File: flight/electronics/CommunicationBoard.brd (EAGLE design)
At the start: 90 x 90 mm, 11 parts, among them J1 CONUFL001-SMD-T, X1 JST-XH-02-PIN

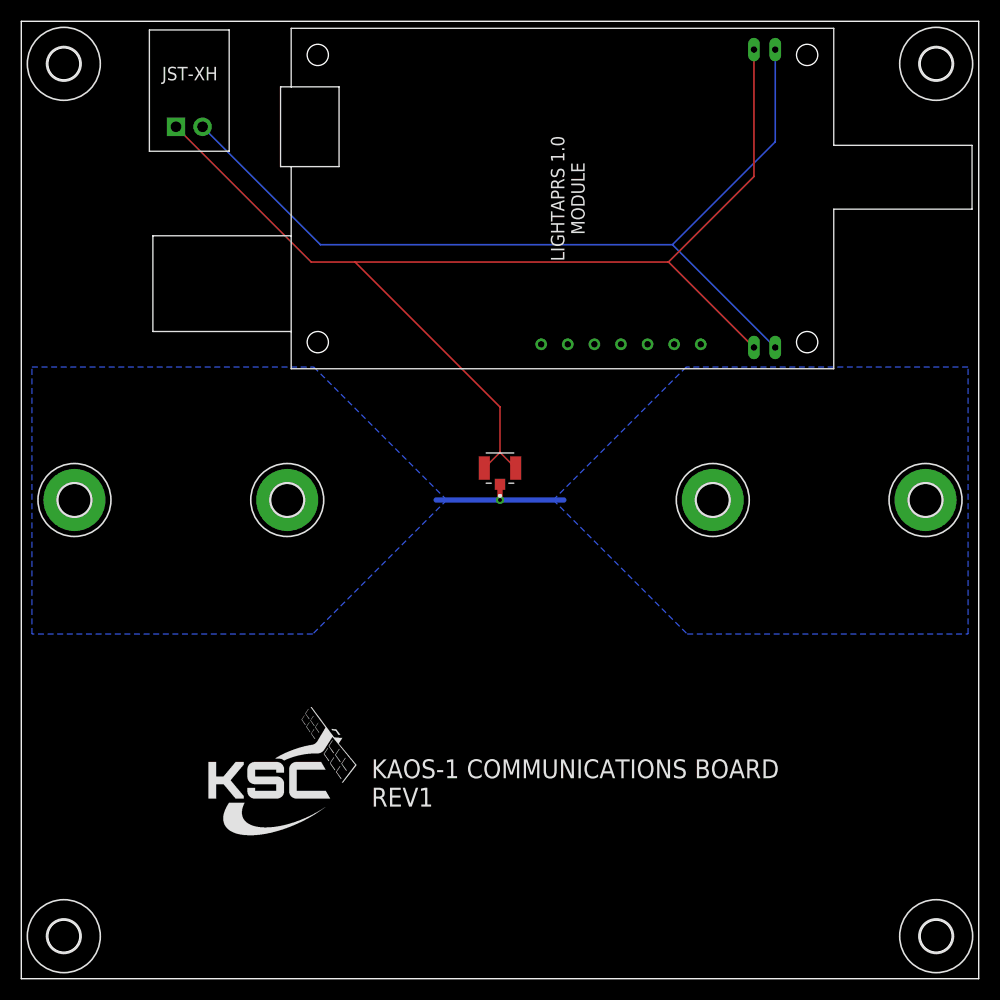
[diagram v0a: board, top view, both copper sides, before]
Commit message: move antenna mounting holes
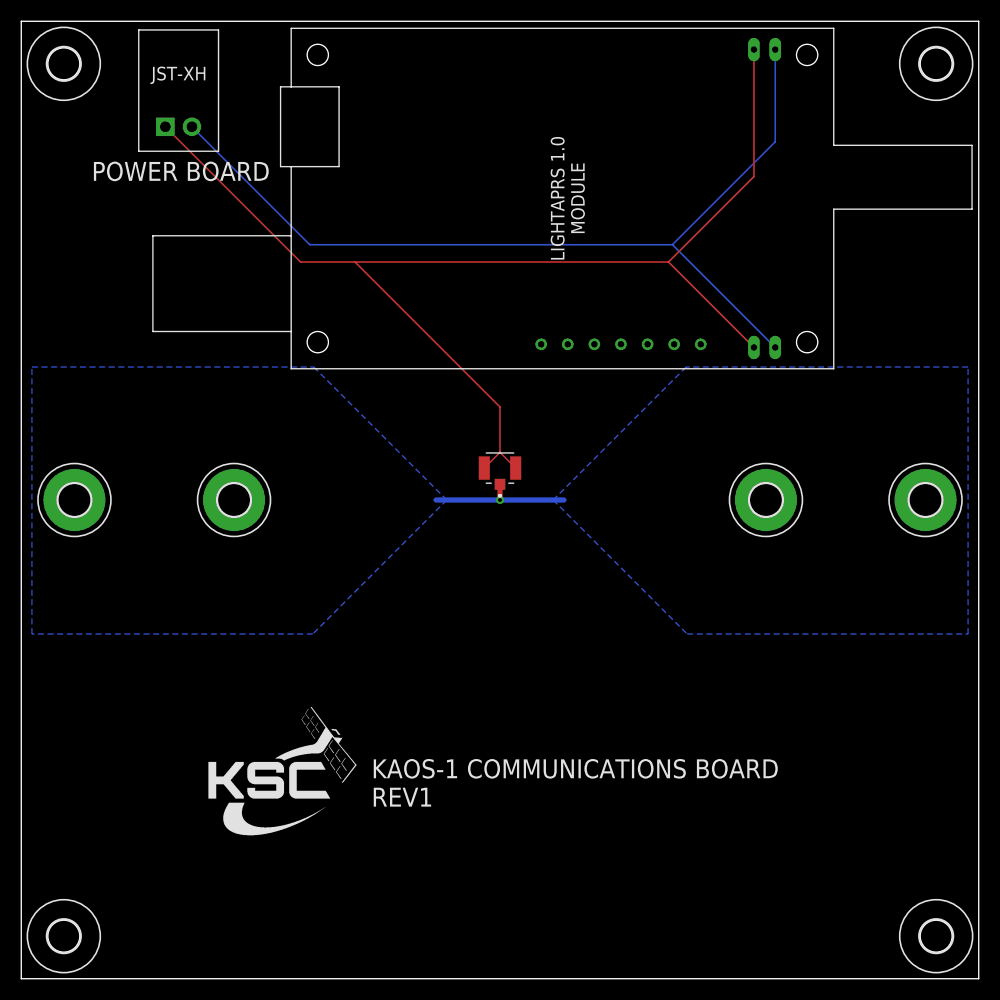
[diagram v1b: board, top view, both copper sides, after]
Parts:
- moved H2 5.00 mm to (70.0, 45.0)
- moved H3 5.00 mm to (20.0, 45.0)
- moved X1 1.00 mm to (13.5, 80.1)
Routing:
- net VBAT: track 84.8 -> 85.8 mm
- net GND: track 113.9 -> 114.9 mm
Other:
- board text added: "POWER BOARD"
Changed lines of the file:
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@@
 <rectangle x1="27.2161" y1="25.4889" x2="27.3177" y2="25.5143" layer="21"/>
 <rectangle x1="27.1907" y1="25.5143" x2="27.3177" y2="25.5397" layer="21"/>
+<text x="15" y="75" size="1.778" layer="21" font="vector" align="bottom-center">POWER BOARD</text>
 </plain>
 <attributes>
@@
 <elements>
 <element name="U$1" library="Breakouts" package="LIGHTAPRS" value="LIGHTAPRS" x="51.372" y="73.3382" smashed="yes" rot="R270"/>
-<element name="X1" library="Rembrandt Electronics - JST XH Connectors v1-0" package="JST-XH_S2B" value="JST-XH-02-PIN" x="14.5424" y="80.0828" smashed="yes"/>
+<element name="X1" library="Rembrandt Electronics - JST XH Connectors v1-0" package="JST-XH_S2B" value="JST-XH-02-PIN" x="13.5424" y="80.0828" smashed="yes"/>
 <element name="J1" library="CONUFL001-SMD-T" package="LINX_CONUFL001-SMD-T" value="CONUFL001-SMD-T" x="45" y="48" smashed="yes">
 <attribute name="AVAILABILITY" value="In Stock" x="45" y="48" size="1.778" layer="27" display="off"/>
@@
 <attribute name="POPULARITY" value="17" x="85" y="45" size="0.0508" layer="27" font="vector" display="off"/>
 </element>
-<element name="H2" library="holes" library_urn="urn:adsk.eagle:library:237" package="3,0-PAD" package3d_urn="urn:adsk.eagle:package:14280/1" value="MOUNT-PAD-ROUND3.0" x="65" y="45" smashed="yes">
-<attribute name="POPULARITY" value="17" x="65" y="45" size="0.0508" layer="27" font="vector" display="off"/>
-</element>
-<element name="H3" library="holes" library_urn="urn:adsk.eagle:library:237" package="3,0-PAD" package3d_urn="urn:adsk.eagle:package:14280/1" value="MOUNT-PAD-ROUND3.0" x="25" y="45" smashed="yes">
-<attribute name="POPULARITY" value="17" x="25" y="45" size="0.0508" layer="27" font="vector" display="off"/>
+<element name="H2" library="holes" library_urn="urn:adsk.eagle:library:237" package="3,0-PAD" package3d_urn="urn:adsk.eagle:package:14280/1" value="MOUNT-PAD-ROUND3.0" x="70" y="45" smashed="yes">
+<attribute name="POPULARITY" value="17" x="70" y="45" size="0.0508" layer="27" font="vector" display="off"/>
+</element>
+<element name="H3" library="holes" library_urn="urn:adsk.eagle:library:237" package="3,0-PAD" package3d_urn="urn:adsk.eagle:package:14280/1" value="MOUNT-PAD-ROUND3.0" x="20" y="45" smashed="yes">
+<attribute name="POPULARITY" value="17" x="20" y="45" size="0.0508" layer="27" font="vector" display="off"/>
 </element>
 <element name="H4" library="holes" library_urn="urn:adsk.eagle:library:237" package="3,0-PAD" package3d_urn="urn:adsk.eagle:package:14280/1" value="MOUNT-PAD-ROUND3.0" x="5" y="45" smashed="yes">
@@
 <contactref element="U$1" pad="GND2"/>
 <contactref element="X1" pad="PIN1"/>
-<wire x1="14.5424" y1="80.0828" x2="27.2552" y2="67.37" width="0.1524" layer="1"/>
+<wire x1="13.5424" y1="80.0828" x2="26.2552" y2="67.37" width="0.1524" layer="1"/>
 <wire x1="31.37" y1="67.37" x2="45" y2="53.74" width="0.1524" layer="1"/>
 <contactref element="J1" pad="3"/>
@@
 <wire x1="46.475" y1="48" x2="45" y2="49.475" width="0.1524" layer="1"/>
 <wire x1="45" y1="49.475" x2="45" y2="53.74" width="0.1524" layer="1"/>
-<wire x1="31.37" y1="67.37" x2="27.2552" y2="67.37" width="0.1524" layer="1"/>
+<wire x1="31.37" y1="67.37" x2="26.2552" y2="67.37" width="0.1524" layer="1"/>
 <wire x1="68.872" y1="59.3382" x2="60.8402" y2="67.37" width="0.1524" layer="1"/>
 <wire x1="60.8402" y1="67.37" x2="31.37" y2="67.37" width="0.1524" layer="1"/>
@@
 <contactref element="U$1" pad="VBAT1"/>
 <contactref element="U$1" pad="VBAT2"/>
-<wire x1="28.1252" y1="69" x2="17.0424" y2="80.0828" width="0.1524" layer="16"/>
-<wire x1="61.2102" y1="69" x2="28.1252" y2="69" width="0.1524" layer="16"/>
+<wire x1="27.1252" y1="69" x2="16.0424" y2="80.0828" width="0.1524" layer="16"/>
+<wire x1="61.2102" y1="69" x2="27.1252" y2="69" width="0.1524" layer="16"/>
 <wire x1="70.872" y1="59.3382" x2="61.2102" y2="69" width="0.1524" layer="16"/>
 <wire x1="70.872" y1="78.6618" x2="61.2102" y2="69" width="0.1524" layer="16"/>

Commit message: round board corners
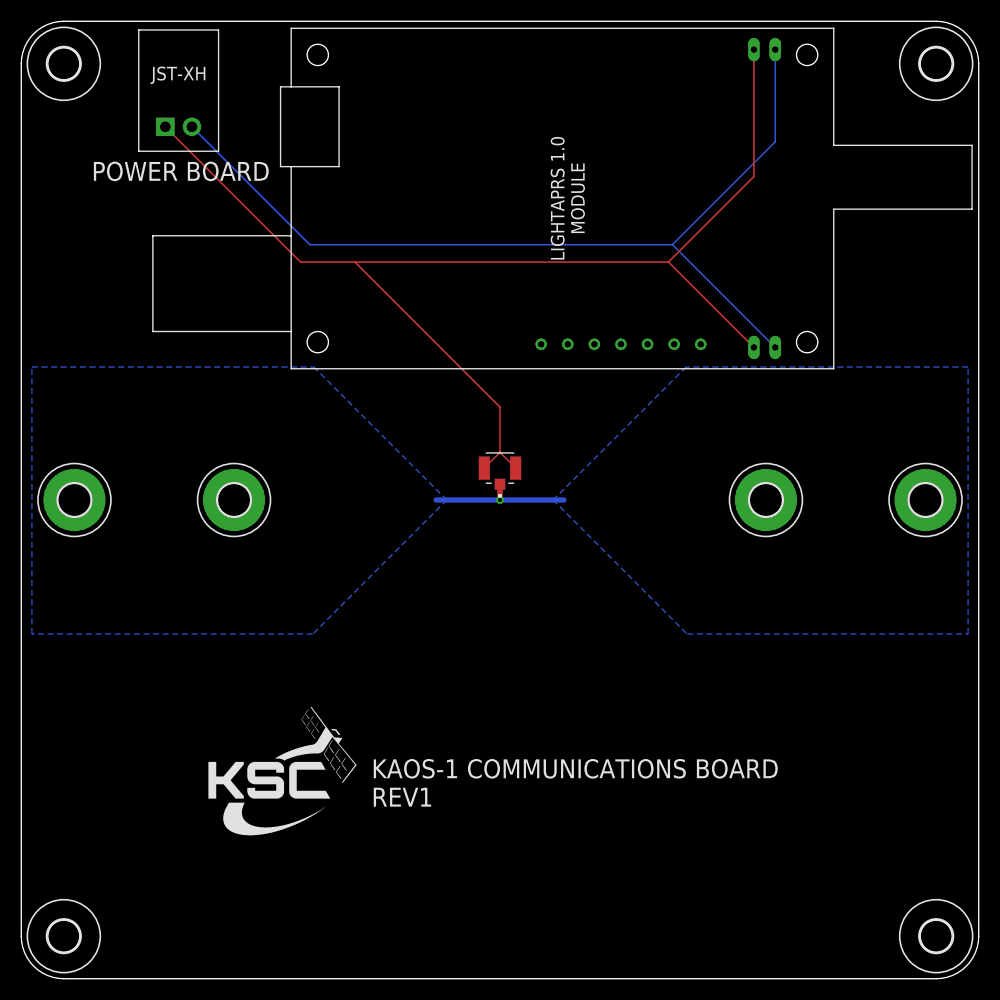
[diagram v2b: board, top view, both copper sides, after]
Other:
- outline, holes or cut-outs redrawn
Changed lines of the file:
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@@
 <board>
 <plain>
-<wire x1="0" y1="0" x2="90" y2="0" width="0" layer="20"/>
-<wire x1="90" y1="0" x2="90" y2="90" width="0" layer="20"/>
-<wire x1="90" y1="90" x2="0" y2="90" width="0" layer="20"/>
-<wire x1="0" y1="90" x2="0" y2="0" width="0" layer="20"/>
+<wire x1="4" y1="0" x2="86" y2="0" width="0" layer="20"/>
+<wire x1="90" y1="4" x2="90" y2="86" width="0" layer="20"/>
+<wire x1="86" y1="90" x2="4" y2="90" width="0" layer="20"/>
 <polygon width="0.2" layer="30">
 <vertex x="1" y="32.4"/>
@@
 <rectangle x1="27.1907" y1="25.5143" x2="27.3177" y2="25.5397" layer="21"/>
 <text x="15" y="75" size="1.778" layer="21" font="vector" align="bottom-center">POWER BOARD</text>
+<wire x1="0" y1="86" x2="0" y2="4" width="0" layer="20"/>
+<wire x1="4" y1="0" x2="0" y2="4" width="0" layer="20" curve="-90"/>
+<wire x1="90" y1="4" x2="86" y2="0" width="0" layer="20" curve="-90"/>
+<wire x1="86" y1="90" x2="90" y2="86" width="0" layer="20" curve="-90"/>
+<wire x1="0" y1="86" x2="4" y2="90" width="0" layer="20" curve="-90"/>
 </plain>
 <attributes>

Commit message: remove thermal isolation
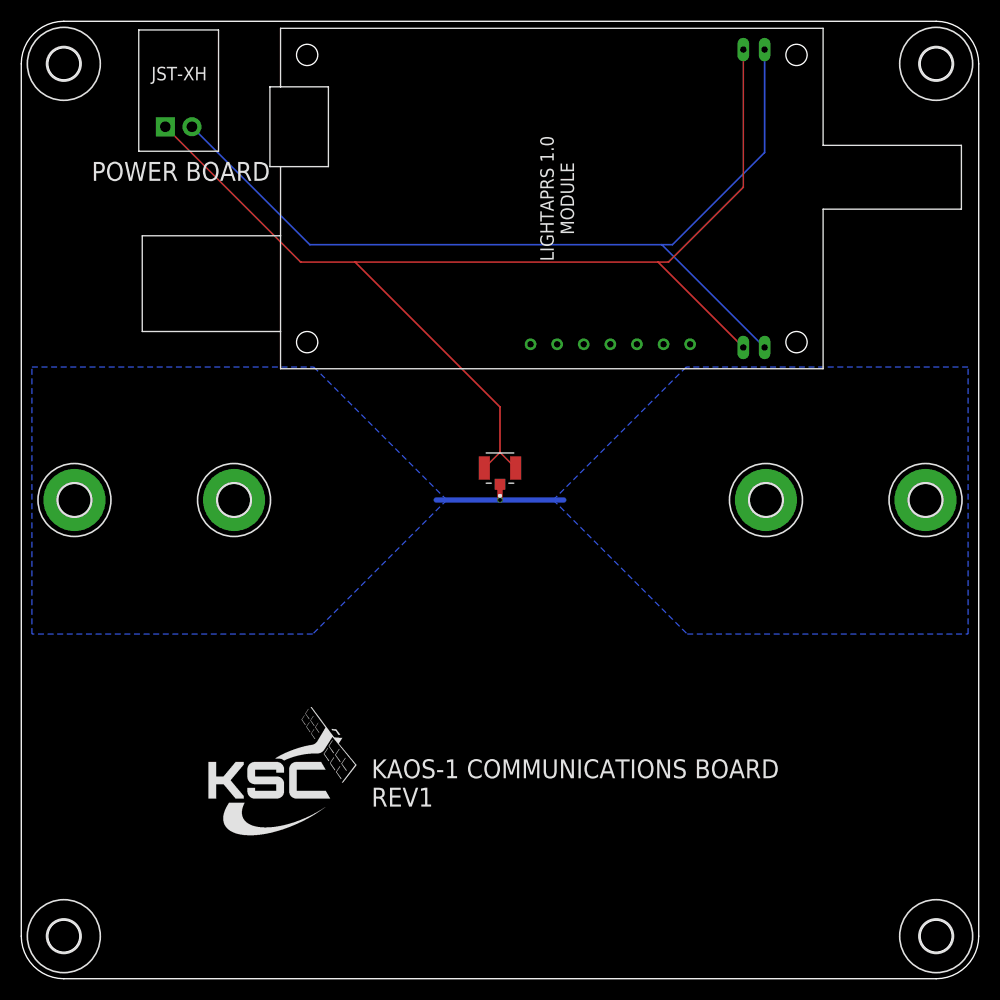
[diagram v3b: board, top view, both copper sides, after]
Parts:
- moved U$1 1.00 mm to (50.4, 73.3)
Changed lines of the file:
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@@
 </class>
 </classes>
-<designrules name="default">
-<description language="de">&lt;b&gt;EAGLE Design Rules&lt;/b&gt;
-&lt;p&gt;
-Die Standard-Design-Rules sind so gewählt, dass sie für
-die meisten Anwendungen passen. Sollte ihre Platine
-besondere Anforderungen haben, treffen Sie die erforderlichen
-Einstellungen hier und speichern die Design Rules unter
-einem neuen Namen ab.</description>
-<description language="en">&lt;b&gt;EAGLE Design Rules&lt;/b&gt;
-&lt;p&gt;
-The default Design Rules have been set to cover
-a wide range of applications. Your particular design
-may have different requirements, so please make the
-necessary adjustments and save your customized
-design rules under a new name.</description>
+<designrules name="jlcpcb-2layers">
+<description language="en">&lt;b&gt;JLCPCB design rules (2 layers)&lt;/b&gt;
+&lt;ul&gt;
+&lt;li&gt;Board thickness: 1.6mm&lt;/li&gt;
+&lt;li&gt;Copper weight: 1oz (35um)&lt;/li&gt;
+&lt;li&gt;Note: annular ring aren't minimal&lt;/li&gt;
+&lt;/ul&gt;</description>
 <param name="layerSetup" value="(1*16)"/>
 <param name="mtCopper" value="0.035mm 0.035mm 0.035mm 0.035mm 0.035mm 0.035mm 0.035mm 0.035mm 0.035mm 0.035mm 0.035mm 0.035mm 0.035mm 0.035mm 0.035mm 0.035mm"/>
-<param name="mtIsolate" value="1.5mm 0.15mm 0.2mm 0.15mm 0.2mm 0.15mm 0.2mm 0.15mm 0.2mm 0.15mm 0.2mm 0.15mm 0.2mm 0.15mm 0.2mm"/>
-<param name="mdWireWire" value="6mil"/>
-<param name="mdWirePad" value="6mil"/>
-<param name="mdWireVia" value="6mil"/>
-<param name="mdPadPad" value="6mil"/>
-<param name="mdPadVia" value="6mil"/>
-<param name="mdViaVia" value="6mil"/>
-<param name="mdSmdPad" value="6mil"/>
-<param name="mdSmdVia" value="6mil"/>
-<param name="mdSmdSmd" value="6mil"/>
+<param name="mtIsolate" value="1.6mm 0.15mm 0.2mm 0.15mm 0.2mm 0.15mm 0.2mm 0.15mm 0.2mm 0.15mm 0.2mm 0.15mm 0.2mm 0.15mm 0.2mm"/>
+<param name="mdWireWire" value="5mil"/>
+<param name="mdWirePad" value="5mil"/>
+<param name="mdWireVia" value="5mil"/>
+<param name="mdPadPad" value="5mil"/>
+<param name="mdPadVia" value="5mil"/>
+<param name="mdViaVia" value="5mil"/>
+<param name="mdSmdPad" value="5mil"/>
+<param name="mdSmdVia" value="5mil"/>
+<param name="mdSmdSmd" value="5mil"/>
 <param name="mdViaViaSameLayer" value="6mil"/>
 <param name="mnLayersViaInSmd" value="2"/>
-<param name="mdCopperDimension" value="40mil"/>
+<param name="mdCopperDimension" value="0.2mm"/>
 <param name="mdDrill" value="6mil"/>
 <param name="mdSmdStop" value="0mil"/>
-<param name="msWidth" value="6mil"/>
-<param name="msDrill" value="0.35mm"/>
-<param name="msMicroVia" value="9.99mm"/>
+<param name="msWidth" value="5mil"/>
+<param name="msDrill" value="0.3mm"/>
+<param name="msMicroVia" value="0.3mm"/>
 <param name="msBlindViaRatio" value="0.5"/>
-<param name="rvPadTop" value="0.25"/>
-<param name="rvPadInner" value="0.25"/>
-<param name="rvPadBottom" value="0.25"/>
-<param name="rvViaOuter" value="0.25"/>
-<param name="rvViaInner" value="0.25"/>
-<param name="rvMicroViaOuter" value="0.25"/>
-<param name="rvMicroViaInner" value="0.25"/>
+<param name="rvPadTop" value="0.4"/>
+<param name="rvPadInner" value="0"/>
+<param name="rvPadBottom" value="0.4"/>
+<param name="rvViaOuter" value="0"/>
+<param name="rvViaInner" value="0"/>
+<param name="rvMicroViaOuter" value="0"/>
+<param name="rvMicroViaInner" value="0"/>
 <param name="rlMinPadTop" value="10mil"/>
-<param name="rlMaxPadTop" value="20mil"/>
+<param name="rlMaxPadTop" value="80mil"/>
 <param name="rlMinPadInner" value="10mil"/>
 <param name="rlMaxPadInner" value="20mil"/>
 <param name="rlMinPadBottom" value="10mil"/>
-<param name="rlMaxPadBottom" value="20mil"/>
-<param name="rlMinViaOuter" value="8mil"/>
+<param name="rlMaxPadBottom" value="80mil"/>
+<param name="rlMinViaOuter" value="3mil"/>
 <param name="rlMaxViaOuter" value="20mil"/>
 <param name="rlMinViaInner" value="8mil"/>
 <param name="rlMaxViaInner" value="20mil"/>
-<param name="rlMinMicroViaOuter" value="4mil"/>
+<param name="rlMinMicroViaOuter" value="3mil"/>
 <param name="rlMaxMicroViaOuter" value="20mil"/>
 <param name="rlMinMicroViaInner" value="4mil"/>
@@
 </autorouter>
 <elements>
-<element name="U$1" library="Breakouts" package="LIGHTAPRS" value="LIGHTAPRS" x="51.372" y="73.3382" smashed="yes" rot="R270"/>
+<element name="U$1" library="Breakouts" package="LIGHTAPRS" value="LIGHTAPRS" x="50.372" y="73.3382" smashed="yes" rot="R270"/>
 <element name="X1" library="Rembrandt Electronics - JST XH Connectors v1-0" package="JST-XH_S2B" value="JST-XH-02-PIN" x="13.5424" y="80.0828" smashed="yes"/>
 <element name="J1" library="CONUFL001-SMD-T" package="LINX_CONUFL001-SMD-T" value="CONUFL001-SMD-T" x="45" y="48" smashed="yes">
@@
 <wire x1="45" y1="49.475" x2="45" y2="53.74" width="0.1524" layer="1"/>
 <wire x1="31.37" y1="67.37" x2="26.2552" y2="67.37" width="0.1524" layer="1"/>
-<wire x1="68.872" y1="59.3382" x2="60.8402" y2="67.37" width="0.1524" layer="1"/>
-<wire x1="60.8402" y1="67.37" x2="31.37" y2="67.37" width="0.1524" layer="1"/>
-<wire x1="68.872" y1="87.3382" x2="68.872" y2="75.4018" width="0.1524" layer="1"/>
-<wire x1="68.872" y1="75.4018" x2="60.8402" y2="67.37" width="0.1524" layer="1"/>
+<wire x1="67.872" y1="59.3382" x2="59.8402" y2="67.37" width="0.1524" layer="1"/>
+<wire x1="60.8402" y1="67.37" x2="59.8402" y2="67.37" width="0.1524" layer="1"/>
+<wire x1="59.8402" y1="67.37" x2="31.37" y2="67.37" width="0.1524" layer="1"/>
+<wire x1="67.872" y1="87.3382" x2="67.872" y2="74.4018" width="0.1524" layer="1"/>
+<wire x1="67.872" y1="74.4018" x2="60.8402" y2="67.37" width="0.1524" layer="1"/>
 </signal>
 <signal name="VBAT">
@@
 <contactref element="U$1" pad="VBAT2"/>
 <wire x1="27.1252" y1="69" x2="16.0424" y2="80.0828" width="0.1524" layer="16"/>
-<wire x1="61.2102" y1="69" x2="27.1252" y2="69" width="0.1524" layer="16"/>
-<wire x1="70.872" y1="59.3382" x2="61.2102" y2="69" width="0.1524" layer="16"/>
-<wire x1="70.872" y1="78.6618" x2="61.2102" y2="69" width="0.1524" layer="16"/>
-<wire x1="70.872" y1="87.3382" x2="70.872" y2="78.6618" width="0.1524" layer="16"/>
+<wire x1="61.2102" y1="69" x2="60.2102" y2="69" width="0.1524" layer="16"/>
+<wire x1="60.2102" y1="69" x2="27.1252" y2="69" width="0.1524" layer="16"/>
+<wire x1="69.872" y1="59.3382" x2="60.2102" y2="69" width="0.1524" layer="16"/>
+<wire x1="69.872" y1="77.6618" x2="61.2102" y2="69" width="0.1524" layer="16"/>
+<wire x1="69.872" y1="87.3382" x2="69.872" y2="77.6618" width="0.1524" layer="16"/>
 </signal>
 <signal name="SIG">
-<polygon width="0.2" layer="16">
+<polygon width="0.2" layer="16" thermals="no">
 <vertex x="1" y="32.4"/>
 <vertex x="1" y="57.5"/>
@@
 <vertex x="27.4" y="32.4"/>
 </polygon>
-<polygon width="0.2" layer="16">
+<polygon width="0.2" layer="16" thermals="no">
 <vertex x="89" y="57.5"/>
 <vertex x="62.5" y="57.5"/>
